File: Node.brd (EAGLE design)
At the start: 38.1 x 38.1 mm, 66 parts, among them J2 DF12A3.0-14DS, Q1 16MHz, U1 ATMEGA32U4QFN, U2 NRF24L01NOPAD, U3 LTC3553, U4 L3GD20, U6 LSM303DLHC, U7 BD2425NNRF0404, U9 RCLAMP0502A, X1 USBSMD

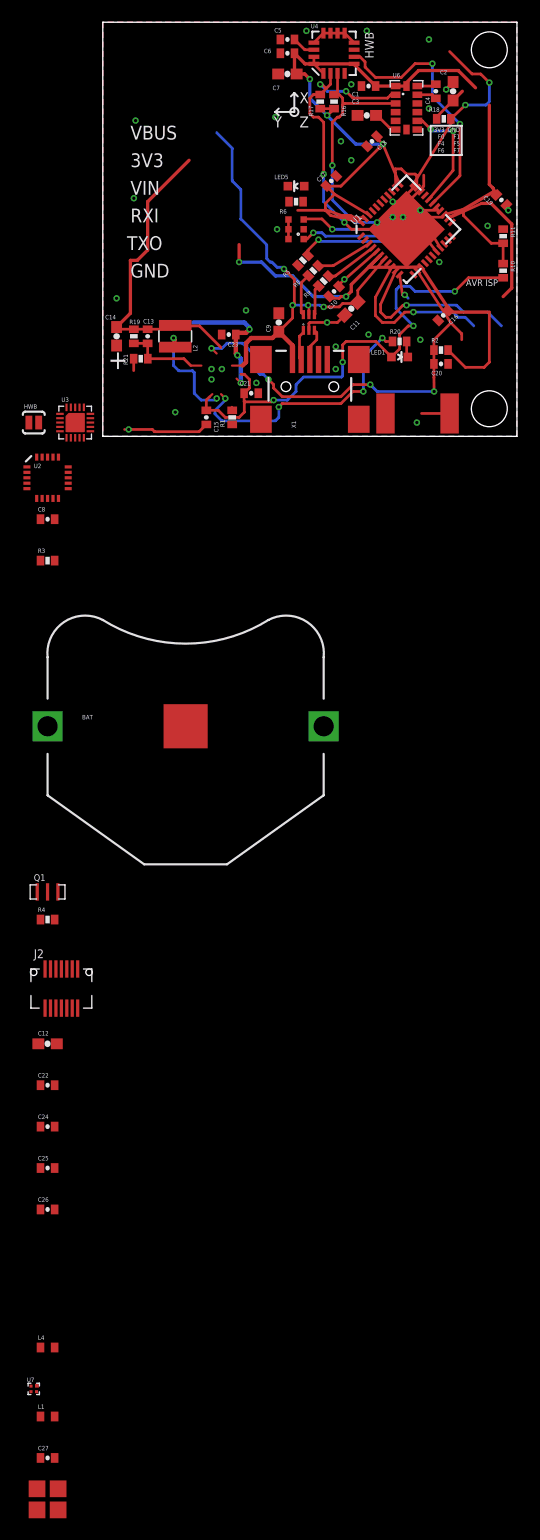
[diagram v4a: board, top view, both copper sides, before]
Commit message: cleanup some names
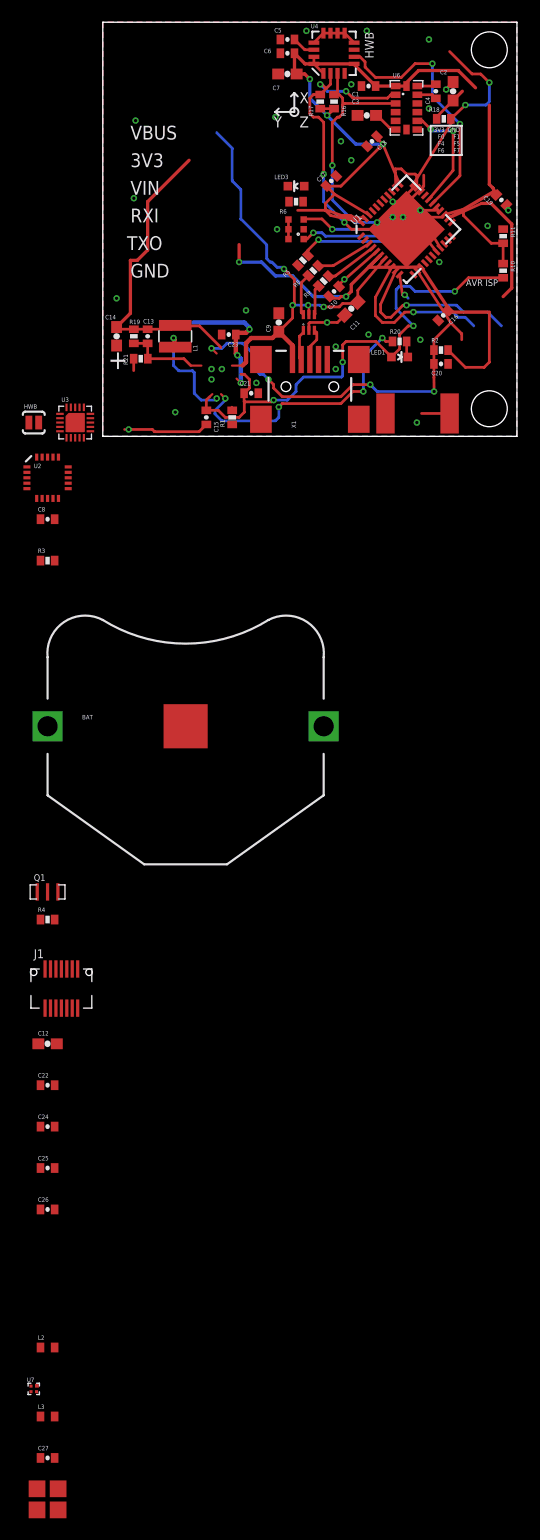
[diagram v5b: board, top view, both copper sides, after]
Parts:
- removed L4: 3.9nH, adjacent-reality:C0402
- added L3: TBD, adjacent-reality:C0402
- L1: value TBD -> 4.7uH; device adjacent-reality:C0402 -> adjacent-reality:VLS30
- L2: value 4.7uH -> 3.9nH; device adjacent-reality:VLS30 -> adjacent-reality:C0402
- moved L1 100.1 mm to (6.67, 9.21), turned to 90 degrees
- moved L2 93.8 mm to (-5.08, -83.8), turned to 0 degrees
- renumbered J2 to J1, LED4 to LED2, LED5 to LED3
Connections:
- net +3V3: now also L1.2; no longer L2.2
- net N$27: now also L1.1; no longer L2.1
- net N$28: now also L2.1; no longer L4.1
- net N$30: now also L3.2; no longer L1.2
- net N$31: now also L2.2, L3.1; no longer L1.1, L4.2

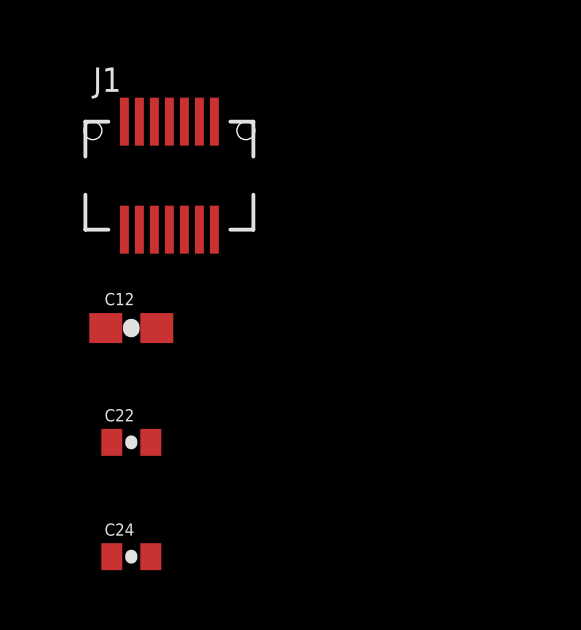
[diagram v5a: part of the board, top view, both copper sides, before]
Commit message: start of base station
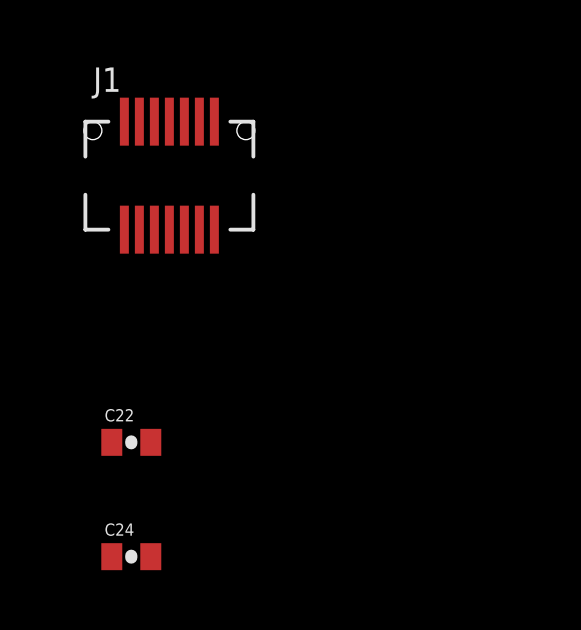
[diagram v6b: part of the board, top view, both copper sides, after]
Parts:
- removed C12: 10uF, SparkFun:0603-CAP
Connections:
- net +3V3: no longer C12.1
- net GND: no longer C12.2
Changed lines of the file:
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@@
 <element name="R4" library="SparkFun" package="0402-RES" value="1M" x="-5.08" y="-44.45"/>
 <element name="J1" library="adjacent-reality" package="DF12A3.0-14DS" value="DF12A3.0-14DS" x="-3.81" y="-50.8"/>
-<element name="C12" library="SparkFun" package="0603-CAP" value="10uF" x="-5.08" y="-55.88"/>
 <element name="C22" library="SparkFun" package="0402-CAP" value="10nF" x="-5.08" y="-59.69"/>
 <element name="C24" library="SparkFun" package="0402-CAP" value="1nF" x="-5.08" y="-63.5"/>
@@
 <contactref element="Q1" pad="P$2"/>
 <contactref element="J1" pad="6"/>
-<contactref element="C12" pad="2"/>
 <contactref element="C22" pad="2"/>
 <contactref element="C24" pad="2"/>
@@
 <wire x1="-4.43" y1="-63.5" x2="-4.43" y2="-67.31" width="0" layer="19" extent="1-1"/>
 <wire x1="-4.43" y1="-59.69" x2="-4.43" y2="-63.5" width="0" layer="19" extent="1-1"/>
-<wire x1="-4.23" y1="-55.88" x2="-4.43" y2="-59.69" width="0" layer="19" extent="1-1"/>
-<wire x1="-3.31" y1="-52.6" x2="-4.23" y2="-55.88" width="0" layer="19" extent="1-1"/>
+<wire x1="-3.31" y1="-52.6" x2="-4.43" y2="-59.69" width="0" layer="19" extent="1-1"/>
 <wire x1="-5.08" y1="-41.91" x2="-3.31" y2="-52.6" width="0" layer="19" extent="1-1"/>
 <wire x1="7.62" y1="-26.67" x2="-5.08" y2="-41.91" width="0" layer="19" extent="1-1"/>
@@
 <contactref element="J1" pad="2"/>
 <contactref element="C24" pad="1"/>
-<contactref element="C12" pad="1"/>
 <contactref element="C22" pad="1"/>
 <wire x1="-5.73" y1="-59.69" x2="-5.73" y2="-63.5" width="0" layer="19" extent="1-1"/>
-<wire x1="-5.93" y1="-55.88" x2="-5.73" y2="-59.69" width="0" layer="19" extent="1-1"/>
-<wire x1="-2.31" y1="-52.6" x2="-5.93" y2="-55.88" width="0" layer="19" extent="1-1"/>
+<wire x1="-2.31" y1="-52.6" x2="-5.73" y2="-59.69" width="0" layer="19" extent="1-1"/>
 <wire x1="-5.58" y1="-5.71" x2="-2.31" y2="-52.6" width="0" layer="19" extent="1-1"/>
 <wire x1="-3.18" y1="-2.81" x2="-5.58" y2="-5.71" width="0" layer="19" extent="1-1"/>

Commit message: usb port parts
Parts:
- X1: value USBSMD -> USB-FCI; device SparkFun:USB-MINIB -> adjacent-reality:USB-MICROB-FCI
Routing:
- net VBUS: track 43.9 -> 47.8 mm
- net D-: track 2.89 -> 6.40 mm
- net D+: track 3.03 -> 6.40 mm
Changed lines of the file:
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@@
 <attribute name="VALUE" x="18.4785" y="32.258" size="0.4064" layer="27" font="vector" rot="R180"/>
 </element>
-<element name="X1" library="SparkFun" package="USB-MINIB" value="USBSMD" x="19.05" y="4.572" rot="R90"/>
+<element name="X1" library="adjacent-reality" package="USB-MICROB-FCI" value="USB-FCI" x="19.05" y="4.572" rot="R90"/>
 <element name="C9" library="SparkFun" package="0603-CAP" value="10uF" x="16.1925" y="10.4775" rot="R90"/>
 <element name="C10" library="SparkFun" package="0402-CAP" value="1uF" x="21.2725" y="13.335" smashed="yes" rot="R45">
@@
 <wire x1="18.9611" y1="10.3886" x2="16.1925" y2="11.3275" width="0" layer="19" extent="1-1"/>
 <wire x1="21.43125" y1="8.255" x2="21.59" y2="10.4775" width="0" layer="19" extent="1-1"/>
-<wire x1="20.65" y1="7.072" x2="21.43125" y2="8.255" width="0" layer="19" extent="1-1"/>
-<wire x1="21.43125" y1="6.19125" x2="20.65" y2="7.072" width="0" layer="19" extent="1-1"/>
+<wire x1="16.375" y1="5.872" x2="21.43125" y2="8.255" width="0" layer="19" extent="1-1"/>
+<wire x1="21.43125" y1="6.19125" x2="16.375" y2="5.872" width="0" layer="19" extent="1-1"/>
 <wire x1="21.73211875" y1="13.79461875" x2="22.25895625" y2="11.14645625" width="0" layer="19" extent="1-1"/>
 <wire x1="22.225" y1="14.44625" x2="21.73211875" y2="13.973490625" width="0" layer="19" extent="1-1"/>
@@
 <wire x1="25.8893875" y1="16.29228125" x2="23.461040625" y2="13.43966875" width="0.254" layer="1"/>
 <wire x1="23.461040625" y1="13.43966875" x2="23.461040625" y2="12.348540625" width="0.254" layer="1"/>
-<wire x1="17.45" y1="7.072" x2="17.45" y2="8.37" width="0.4064" layer="1"/>
+<wire x1="16.375" y1="3.272" x2="17.45" y2="8.37" width="0.4064" layer="1"/>
 <wire x1="17.45" y1="8.37" x2="16.1925" y2="9.6275" width="0.4064" layer="1"/>
 <wire x1="13.6525" y1="9.04875" x2="15.61375" y2="9.04875" width="0.4064" layer="1"/>
@@
 <contactref element="X1" pad="D-"/>
 <contactref element="U9" pad="1"/>
-<wire x1="18.25" y1="7.072" x2="18.0975" y2="7.2245" width="0.254" layer="1"/>
+<wire x1="16.375" y1="3.922" x2="18.0975" y2="7.2245" width="0.254" layer="1"/>
 <wire x1="18.0975" y1="7.2245" x2="18.0975" y2="9.2075" width="0.254" layer="1"/>
 <wire x1="18.0975" y1="9.2075" x2="18.4531" y2="9.5631" width="0.254" layer="1"/>
@@
 <contactref element="X1" pad="D+"/>
 <contactref element="U9" pad="3"/>
-<wire x1="19.05" y1="7.072" x2="19.05" y2="8.255" width="0.254" layer="1"/>
+<wire x1="16.375" y1="4.572" x2="19.05" y2="8.255" width="0.254" layer="1"/>
 <wire x1="19.05" y1="8.255" x2="19.685" y2="8.89" width="0.254" layer="1"/>
 <wire x1="19.685" y1="8.89" x2="19.685" y2="9.5377" width="0.254" layer="1"/>

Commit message: pin header for base station
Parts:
- removed C20: 100nF, SparkFun:0402-CAP
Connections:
- net GND: no longer C20.2
- net RESET: no longer C20.1
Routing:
- net RESET: track 39.7 -> 10.8 mm, vias 4 -> 0
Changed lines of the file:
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@@
 <attribute name="VALUE" x="31.46425" y="8.6995" size="0.4064" layer="27"/>
-</element>
-<element name="C20" library="SparkFun" package="0402-CAP" value="100nF" x="31.115" y="6.6675" smashed="yes">
-<attribute name="NAME" x="30.226" y="5.61975" size="0.4064" layer="25"/>
-<attribute name="VALUE" x="31.623" y="5.68325" size="0.4064" layer="27"/>
 </element>
 <element name="R16" library="SparkFun" package="0402-RES" value="4.7k" x="21.2725" y="30.7975" smashed="yes" rot="R270">
@@
 <contactref element="C19" pad="2"/>
 <contactref element="C10" pad="2"/>
-<contactref element="C20" pad="2"/>
 <contactref element="U9" pad="2"/>
 <wire x1="19.4225" y1="36.2175" x2="20.2975" y2="37.0925" width="0.254" layer="1"/>
@@
 <wire x1="14.3025" y1="3.96875" x2="11.90625" y2="1.09625" width="0" layer="19" extent="1-1"/>
 <wire x1="14.12875" y1="4.92125" x2="14.3025" y2="3.96875" width="0" layer="19" extent="1-1"/>
+<wire x1="16.375" y1="5.872" x2="14.12875" y2="4.92125" width="0" layer="19" extent="1-1"/>
 <wire x1="10.95375" y1="6.19125" x2="14.12875" y2="4.92125" width="0" layer="19" extent="1-1"/>
 <wire x1="10.00125" y1="6.19125" x2="10.95375" y2="6.19125" width="0" layer="19" extent="1-1"/>
@@
 <wire x1="18.9611" y1="10.3886" x2="16.1925" y2="11.3275" width="0" layer="19" extent="1-1"/>
 <wire x1="21.43125" y1="8.255" x2="21.59" y2="10.4775" width="0" layer="19" extent="1-1"/>
-<wire x1="16.375" y1="5.872" x2="21.43125" y2="8.255" width="0" layer="19" extent="1-1"/>
-<wire x1="21.43125" y1="6.19125" x2="16.375" y2="5.872" width="0" layer="19" extent="1-1"/>
+<wire x1="21.43125" y1="6.19125" x2="21.43125" y2="8.255" width="0" layer="19" extent="1-1"/>
 <wire x1="21.73211875" y1="13.79461875" x2="22.25895625" y2="11.14645625" width="0" layer="19" extent="1-1"/>
 <wire x1="22.225" y1="14.44625" x2="21.73211875" y2="13.973490625" width="0" layer="19" extent="1-1"/>
@@
 <wire x1="29.21" y1="8.89" x2="24.4475" y2="9.36625" width="0" layer="19" extent="1-1"/>
 <wire x1="30.858578125" y1="10.665578125" x2="29.21" y2="8.89" width="0" layer="19" extent="1-1"/>
-<wire x1="31.765" y1="6.6675" x2="29.21" y2="8.89" width="0" layer="19" extent="1-1"/>
 <wire x1="2.8425" y1="6.0475" x2="6.6675" y2="2.2225" width="0" layer="19" extent="1-1"/>
 <wire x1="1.27" y1="8.3575" x2="2.8425" y2="7.14375" width="0" layer="19" extent="1-1"/>
 <wire x1="1.27" y1="12.7" x2="1.27" y2="8.3575" width="0" layer="19" extent="1-1"/>
-<wire x1="28.8925" y1="1.27" x2="31.765" y2="6.6675" width="0" layer="19" extent="1-1"/>
-<wire x1="26.006" y1="2.1082" x2="28.8925" y2="1.27" width="0" layer="19" extent="1-1"/>
+<wire x1="26.006" y1="2.1082" x2="21.43125" y2="6.19125" width="0" layer="19" extent="1-1"/>
+<wire x1="28.8925" y1="1.27" x2="26.006" y2="2.1082" width="0" layer="19" extent="1-1"/>
 <wire x1="16.03375" y1="19.05" x2="22.1445125" y2="20.32" width="0" layer="19" extent="1-1"/>
 <wire x1="2.8575" y1="21.9075" x2="1.27" y2="12.7" width="0" layer="19" extent="1-1"/>
@@
 <signal name="RESET">
 <contactref element="R2" pad="1"/>
-<contactref element="C20" pad="1"/>
 <contactref element="U1" pad="13"/>
-<wire x1="10.4775" y1="7.62" x2="10.00125" y2="8.09625" width="0.2032" layer="1"/>
-<via x="10.00125" y="8.09625" extent="1-16" drill="0.3"/>
-<wire x1="10.00125" y1="8.09625" x2="10.95375" y2="8.09625" width="0.254" layer="16"/>
-<wire x1="10.95375" y1="8.09625" x2="11.43" y2="8.5725" width="0.254" layer="16"/>
-<wire x1="11.43" y1="8.5725" x2="12.85875" y2="8.5725" width="0.254" layer="16"/>
-<wire x1="12.85875" y1="8.5725" x2="13.97" y2="7.46125" width="0.254" layer="16"/>
-<wire x1="13.97" y1="7.46125" x2="13.97" y2="6.19125" width="0.254" layer="16"/>
-<wire x1="13.97" y1="6.19125" x2="14.44625" y2="5.715" width="0.254" layer="16"/>
-<wire x1="14.44625" y1="5.715" x2="14.76375" y2="5.715" width="0.254" layer="16"/>
-<wire x1="14.76375" y1="5.715" x2="15.24" y2="5.23875" width="0.254" layer="16"/>
-<via x="15.24" y="5.23875" extent="1-16" drill="0.3"/>
-<wire x1="30.465" y1="7.9375" x2="30.465" y2="6.6675" width="0.254" layer="1"/>
 <wire x1="28.929946875" y1="15.231621875" x2="32.02725625" y2="10.43725625" width="0.254" layer="1"/>
 <wire x1="32.02725625" y1="10.43725625" x2="33.02" y2="9.4445125" width="0.254" layer="1"/>
-<wire x1="15.24" y1="5.23875" x2="15.71625" y2="4.7625" width="0.254" layer="1"/>
-<wire x1="15.71625" y1="4.7625" x2="15.71625" y2="4.445" width="0.254" layer="1"/>
-<wire x1="15.71625" y1="4.445" x2="16.51" y2="3.65125" width="0.254" layer="1"/>
-<wire x1="16.51" y1="3.65125" x2="21.9075" y2="3.65125" width="0.254" layer="1"/>
-<wire x1="21.9075" y1="3.65125" x2="23.01875" y2="4.7625" width="0.254" layer="1"/>
-<wire x1="23.01875" y1="4.7625" x2="24.60625" y2="4.7625" width="0.254" layer="1"/>
-<via x="24.60625" y="4.7625" extent="1-16" drill="0.3"/>
-<wire x1="24.60625" y1="4.7625" x2="25.24125" y2="4.1275" width="0.254" layer="16"/>
-<wire x1="25.24125" y1="4.1275" x2="30.48" y2="4.1275" width="0.254" layer="16"/>
-<via x="30.48" y="4.1275" extent="1-16" drill="0.3"/>
-<wire x1="30.48" y1="4.1275" x2="30.465" y2="5.4125" width="0.254" layer="1"/>
-<wire x1="30.465" y1="5.4125" x2="30.465" y2="6.6675" width="0.254" layer="1"/>
 <wire x1="33.02" y1="9.4445125" x2="33.02" y2="8.89" width="0.254" layer="1"/>
 <wire x1="30.465" y1="7.9375" x2="30.465" y2="8.875" width="0.254" layer="1"/>
 <wire x1="30.465" y1="8.875" x2="32.02725625" y2="10.43725625" width="0.254" layer="1"/>
 <contactref element="J1" pad="5"/>
-<wire x1="16.51" y1="3.65125" x2="-3.31" y2="-49" width="0" layer="19" extent="1-1"/>
+<wire x1="30.465" y1="7.9375" x2="-3.31" y2="-49" width="0" layer="19" extent="1-1"/>
 </signal>
 <signal name="SCK">
